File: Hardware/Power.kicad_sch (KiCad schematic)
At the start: 43 parts, among them J2 S2B-PH-SM4-TB, Q1 DMP3099L, Q2 2N7002, Q3 2N7002, SW4 KMR231NG, SW5 KSS3xxGx, U2 AP2112K-3.3, U3 BQ21040DBV

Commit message: sch: flip battery connector. The connector did not align with the pinout of the battery, requiring us to flip the connector. CAUTION: If upgrading from Terra X01 to X02, flip back the connector leads on your battery!
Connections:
- net GND: now also J2.2 (Pin_2); no longer J2.1 (Pin_1)
- net VBAT: now also J2.1 (Pin_1); no longer J2.2 (Pin_2)
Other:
- moved on the sheet: J2
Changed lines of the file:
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@@
 	(wire
 		(pts
-			(xy 44.45 101.6) (xy 44.45 102.87)
-		)
-		(stroke
-			(width 0)
-			(type default)
-		)
-	)
-	(wire
-		(pts
 			(xy 147.32 110.49) (xy 147.32 114.3)
 		)
@@
 	(wire
 		(pts
-			(xy 49.53 101.6) (xy 44.45 101.6)
-		)
-		(stroke
-			(width 0)
-			(type default)
-		)
-	)
-	(wire
-		(pts
 			(xy 68.58 132.08) (xy 68.58 133.35)
 		)
@@
 	(wire
 		(pts
-			(xy 49.53 102.87) (xy 49.53 101.6)
-		)
-		(stroke
-			(width 0)
-			(type default)
-		)
-	)
-	(wire
-		(pts
 			(xy 182.88 52.07) (xy 185.42 52.07)
 		)
@@
 	(symbol
 		(lib_id "Connector_Generic_MountingPin:Conn_01x02_MountingPin")
-		(at 49.53 110.49 180)
+		(at 49.53 107.95 0)
+		(mirror y)
 		(unit 1)
 		(exclude_from_sim no)
@@
 		(dnp no)
 		(property "Reference" "J2"
-			(at 46.99 110.1345 0)
+			(at 46.99 108.3055 0)
 			(effects
 				(font
@@
 		)
 		(property "Value" "S2B-PH-SM4-TB"
-			(at 46.99 107.5945 0)
+			(at 46.99 110.8455 0)
 			(effects
 				(font
@@
 		)
 		(property "Footprint" "Connector_JST:JST_PH_S2B-PH-SM4-TB_1x02-1MP_P2.00mm_Horizontal"
-			(at 49.53 110.49 0)
+			(at 49.53 107.95 0)
 			(effects
 				(font
@@
 		)
 		(property "Datasheet" "~"
-			(at 49.53 110.49 0)
+			(at 49.53 107.95 0)
 			(effects
 				(font
@@
 		)
 		(property "Description" "Generic connectable mounting pin connector, single row, 01x02, script generated (kicad-library-utils/schlib/autogen/connector/)"
-			(at 49.53 110.49 0)
+			(at 49.53 107.95 0)
 			(effects
 				(font
@@
 		)
 		(property "MPN" "S2B-PH-SM4-TB"
-			(at 49.53 110.49 0)
+			(at 49.53 107.95 0)
 			(effects
 				(font
@@
 		)
 		(instances
-			(project ""
+			(project "Terra-HW"
 				(path "/acca4a2f-1cc7-44b0-a26a-921257f6c268/5f0d062d-9fa8-4c48-be05-0b92e4e6324b"
 					(reference "J2")
@@
 	(symbol
 		(lib_id "power:GND")
-		(at 44.45 102.87 0)
+		(at 49.53 115.57 0)
 		(unit 1)
 		(exclude_from_sim no)
@@
 		(fields_autoplaced yes)
 		(property "Reference" "#PWR023"
-			(at 44.45 109.22 0)
+			(at 49.53 121.92 0)
 			(effects
 				(font
@@
 		)
 		(property "Value" "GND"
-			(at 44.45 107.95 0)
+			(at 49.53 120.65 0)
 			(effects
 				(font
@@
 		)
 		(property "Footprint" ""
-			(at 44.45 102.87 0)
+			(at 49.53 115.57 0)
 			(effects
 				(font
@@
 		)
 		(property "Datasheet" ""
-			(at 44.45 102.87 0)
+			(at 49.53 115.57 0)
 			(effects
 				(font
@@
 		)
 		(property "Description" "Power symbol creates a global label with name \"GND\" , ground"
-			(at 44.45 102.87 0)
+			(at 49.53 115.57 0)
 			(effects
 				(font

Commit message: sch: replace gps for TESSO-LIV3R
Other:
- note added: "TODO: Fix shutdown issue from stray voltage at this node."
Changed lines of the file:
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@@
+		)
+	)
+	(text "TODO: Fix shutdown issue from stray voltage at this node."
+		(exclude_from_sim no)
+		(at 116.332 38.862 0)
+		(effects
+			(font
+				(size 1.27 1.27)
+				(thickness 0.254)
+				(bold yes)
+				(color 255 153 0 1)
+			)
 		)
 	)

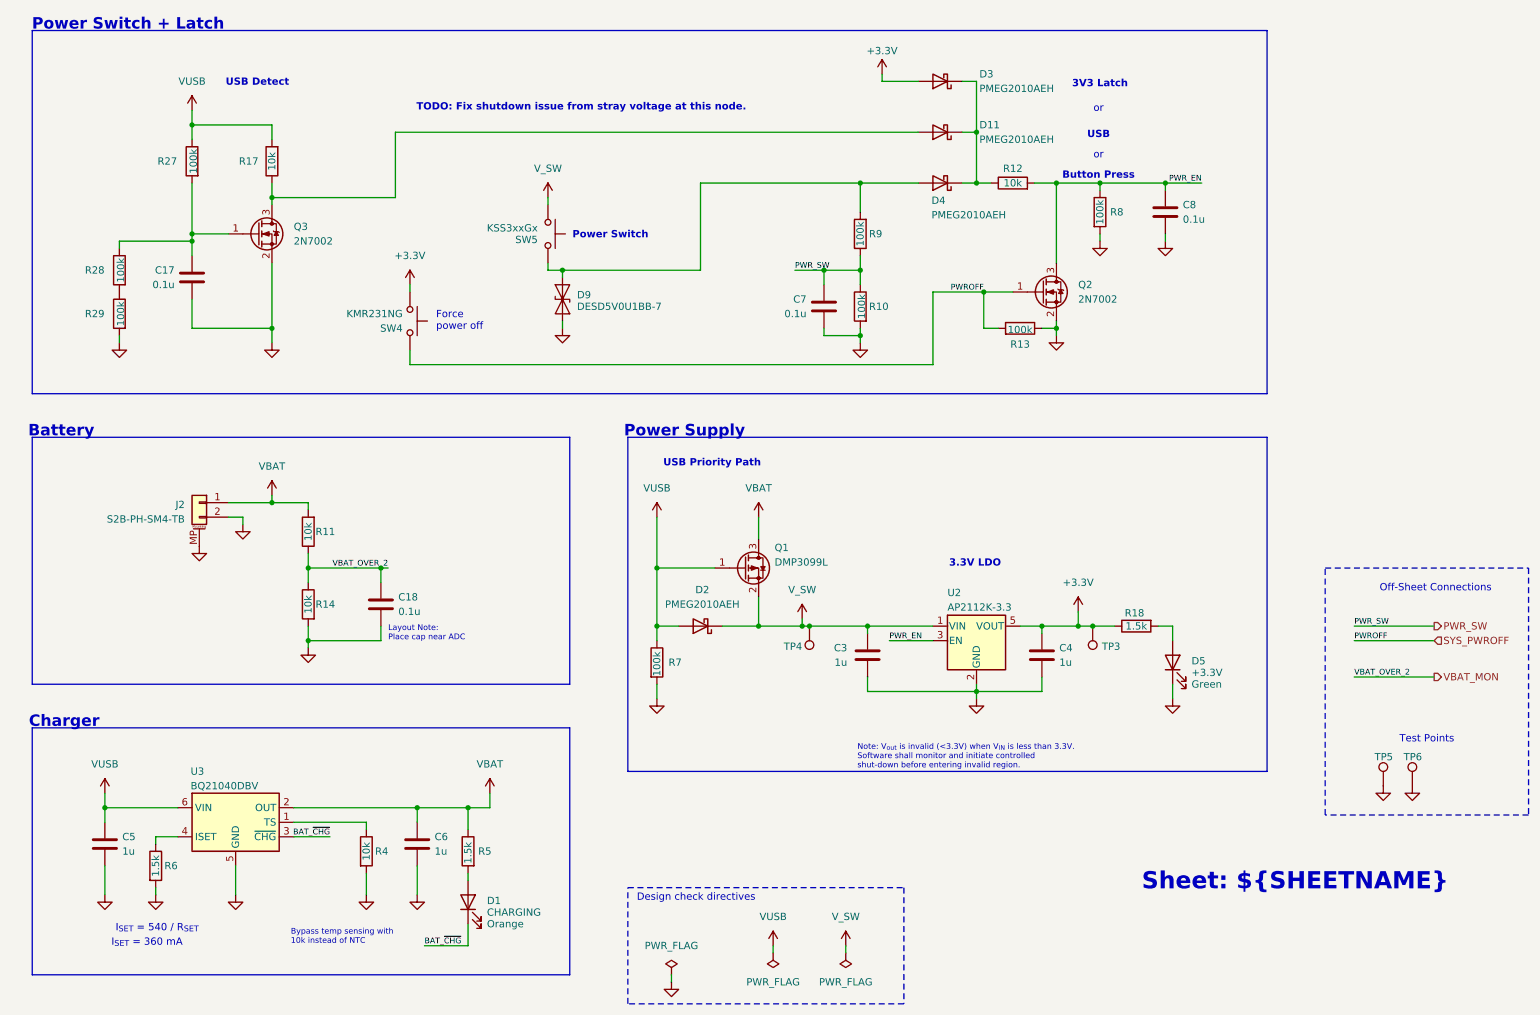
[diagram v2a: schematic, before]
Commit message: sch: change USB Detect to SN74LVC1G14
Removed N-FET used, which had a problem of restarting the device
after powerdown when only powered by battery (no USB)
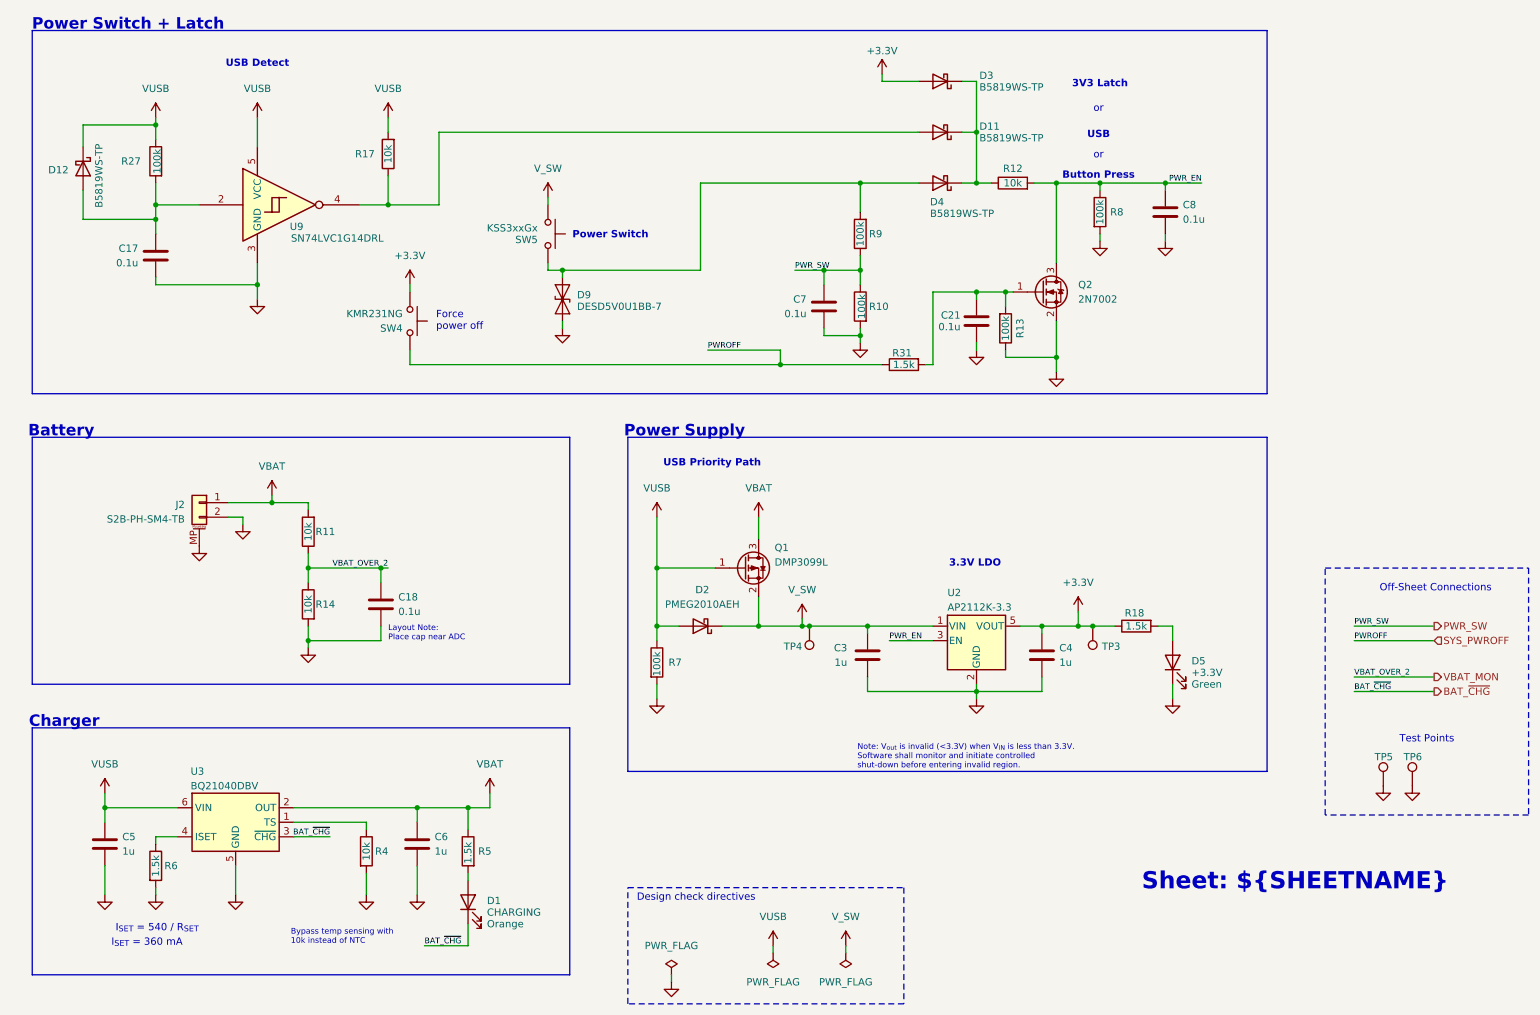
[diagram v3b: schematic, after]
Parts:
- removed Q3: 2N7002, Package_TO_SOT_SMD:SOT-23, symbol Transistor_FET:2N7002
- removed R28, R29: 100k, Resistor_SMD:R_0603_1608Metric, symbol Device:R
- added C21: 0.1u, Capacitor_SMD:C_0603_1608Metric, symbol Device:C
- added D12: B5819WS-TP, Diode_SMD:D_SOD-323, symbol Diode:MBR0520
- added R31: 1.5k, Resistor_SMD:R_0603_1608Metric, symbol Device:R
- added U9: SN74LVC1G14DRL, Package_TO_SOT_SMD:SOT-553, symbol 74xGxx:SN74LVC1G14DRL
- D11, D3, D4: value PMEG2010AEH -> B5819WS-TP; footprint Diode_SMD:D_SOD-123 -> Diode_SMD:D_SOD-323; MPN PMEG2010AEH -> B5819WS-TP
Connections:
- net GND: now also C21.2, U9.3 (GND)
- net SYS_PWROFF: now also R31.1; no longer Q2.1 (G), R13.2
- net VUSB: now also D12.1 (K), U9.5 (VCC)
- net at C17.1, R27.2: now also D12.2 (A), U9.2
- net at D11.2 (A), R17.1: now also U9.4
- new net: C21.1, Q2.1 (G), R13.2, R31.2
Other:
- note removed: "TODO: Fix shutdown issue from stray voltage at this node."
- moved on the sheet: R13

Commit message: sch: updates
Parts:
- R11, R14: value 10k -> 100k; MPN RC0603FR-0710KL -> RC0603FR-07100KL
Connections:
- net GND: now also R14.1; no longer R14.2
- net VBAT_MON: now also R14.2; no longer R14.1
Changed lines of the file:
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@@
 	(title_block
 		(title "${TITLE}")
-		(date "2025-04-06")
+		(date "2025-08-29")
 		(rev "${REVISION}")
 		(company "${COMPANY}")
@@
 	)
 	(symbol
-		(lib_id "Device:R")
-		(at 68.58 125.73 0)
-		(mirror y)
-		(unit 1)
-		(exclude_from_sim no)
-		(in_bom yes)
-		(on_board yes)
-		(dnp no)
-		(property "Reference" "R14"
-			(at 69.85 125.73 0)
-			(effects
-				(font
-					(size 1.27 1.27)
-				)
-				(justify right)
-			)
-		)
-		(property "Value" "10k"
-			(at 68.58 125.73 90)
-			(effects
-				(font
-					(size 1.27 1.27)
-				)
-			)
-		)
-		(property "Footprint" "Resistor_SMD:R_0603_1608Metric"
-			(at 70.358 125.73 90)
-			(effects
-				(font
-					(size 1.27 1.27)
-				)
-				(hide yes)
-			)
-		)
-		(property "Datasheet" "https://www.lcsc.com/datasheet/lcsc_datasheet_2304140030_YAGEO-RC0603FR-071KL_C22548.pdf"
-			(at 68.58 125.73 0)
-			(effects
-				(font
-					(size 1.27 1.27)
-				)
-				(hide yes)
-			)
-		)
-		(property "Description" "Resistor"
-			(at 68.58 125.73 0)
-			(effects
-				(font
-					(size 1.27 1.27)
-				)
-				(hide yes)
-			)
-		)
-		(property "MPN" "RC0603FR-0710KL"
-			(at 68.58 125.73 0)
-			(effects
-				(font
-					(size 1.27 1.27)
-				)
-				(hide yes)
-			)
-		)
-		(pin "1"
-		)
-		(pin "2"
-		)
-		(instances
-			(project "Terra-HW"
-				(path "/acca4a2f-1cc7-44b0-a26a-921257f6c268/5f0d062d-9fa8-4c48-be05-0b92e4e6324b"
-					(reference "R14")
-					(unit 1)
-				)
-			)
-		)
-	)
-	(symbol
 		(lib_id "power:VBUS")
 		(at 129.54 110.49 0)
@@
 	)
 	(symbol
+		(lib_id "Device:R")
+		(at 68.58 125.73 180)
+		(unit 1)
+		(exclude_from_sim no)
+		(in_bom yes)
+		(on_board yes)
+		(dnp no)
+		(property "Reference" "R14"
+			(at 70.104 125.73 0)
+			(effects
+				(font
+					(size 1.27 1.27)
+				)
+				(justify right)
+			)
+		)
+		(property "Value" "100k"
+			(at 68.58 125.73 90)
+			(effects
+				(font
+					(size 1.27 1.27)
+				)
+			)
+		)
+		(property "Footprint" "Resistor_SMD:R_0603_1608Metric"
+			(at 70.358 125.73 90)
+			(effects
+				(font
+					(size 1.27 1.27)
+				)
+				(hide yes)
+			)
+		)
+		(property "Datasheet" "https://www.lcsc.com/datasheet/lcsc_datasheet_2304140030_YAGEO-RC0603FR-071KL_C22548.pdf"
+			(at 68.58 125.73 0)
+			(effects
+				(font
+					(size 1.27 1.27)
+				)
+				(hide yes)
+			)
+		)
+		(property "Description" "Resistor"
+			(at 68.58 125.73 0)
+			(effects
+				(font
+					(size 1.27 1.27)
+				)
+				(hide yes)
+			)
+		)
+		(property "MPN" "RC0603FR-07100KL"
+			(at 68.58 125.73 0)
+			(effects
+				(font
+					(size 1.27 1.27)
+				)
+				(hide yes)
+			)
+		)
+		(pin "1"
+		)
+		(pin "2"
+		)
+		(instances
+			(project "Terra-HW"
+				(path "/acca4a2f-1cc7-44b0-a26a-921257f6c268/5f0d062d-9fa8-4c48-be05-0b92e4e6324b"
+					(reference "R14")
+					(unit 1)
+				)
+			)
+		)
+	)
+	(symbol
 		(lib_id "Diode:MBR0520")
 		(at 179.07 43.18 180)
@@
 	)
 	(symbol
+		(lib_id "Device:R")
+		(at 68.58 113.03 180)
+		(unit 1)
+		(exclude_from_sim no)
+		(in_bom yes)
+		(on_board yes)
+		(dnp no)
+		(property "Reference" "R11"
+			(at 70.104 113.03 0)
+			(effects
+				(font
+					(size 1.27 1.27)
+				)
+				(justify right)
+			)
+		)
+		(property "Value" "100k"
+			(at 68.58 113.03 90)
+			(effects
+				(font
+					(size 1.27 1.27)
+				)
+			)
+		)
+		(property "Footprint" "Resistor_SMD:R_0603_1608Metric"
+			(at 70.358 113.03 90)
+			(effects
+				(font
+					(size 1.27 1.27)
+				)
+				(hide yes)
+			)
+		)
+		(property "Datasheet" "https://www.lcsc.com/datasheet/lcsc_datasheet_2304140030_YAGEO-RC0603FR-071KL_C22548.pdf"
+			(at 68.58 113.03 0)
+			(effects
+				(font
+					(size 1.27 1.27)
+				)
+				(hide yes)
+			)
+		)
+		(property "Description" "Resistor"
+			(at 68.58 113.03 0)
+			(effects
+				(font
+					(size 1.27 1.27)
+				)
+				(hide yes)
+			)
+		)
+		(property "MPN" "RC0603FR-07100KL"
+			(at 68.58 113.03 0)
+			(effects
+				(font
+					(size 1.27 1.27)
+				)
+				(hide yes)
+			)
+		)
+		(pin "1"
+		)
+		(pin "2"
+		)
+		(instances
+			(project "Terra-HW"
+				(path "/acca4a2f-1cc7-44b0-a26a-921257f6c268/5f0d062d-9fa8-4c48-be05-0b92e4e6324b"
+					(reference "R11")
+					(unit 1)
+				)
+			)
+		)
+	)
+	(symbol
 		(lib_id "power:GND")
 		(at 49.53 115.57 0)
@@
 					(unit 1)
 				)
-			)
-		)
-	)
-	(symbol
-		(lib_id "Device:R")
-		(at 68.58 113.03 180)
-		(unit 1)
-		(exclude_from_sim no)
-		(in_bom yes)
-		(on_board yes)
-		(dnp no)
-		(property "Reference" "R11"
-			(at 69.85 113.03 0)
-			(effects
-				(font
-					(size 1.27 1.27)
-				)
-				(justify right)
-			)
-		)
-		(property "Value" "10k"
-			(at 68.58 113.03 90)
-			(effects
-				(font
-					(size 1.27 1.27)
-				)
-			)
-		)
-		(property "Footprint" "Resistor_SMD:R_0603_1608Metric"
-			(at 70.358 113.03 90)
-			(effects
-				(font
-					(size 1.27 1.27)
-				)
-				(hide yes)
-			)
-		)
-		(property "Datasheet" "https://www.lcsc.com/datasheet/lcsc_datasheet_2304140030_YAGEO-RC0603FR-071KL_C22548.pdf"
-			(at 68.58 113.03 0)
-			(effects
-				(font
-					(size 1.27 1.27)
-				)
-				(hide yes)
-			)
-		)
-		(property "Description" "Resistor"
-			(at 68.58 113.03 0)
-			(effects
-				(font
-					(size 1.27 1.27)
-				)
-				(hide yes)
-			)
-		)
-		(property "MPN" "RC0603FR-0710KL"
-			(at 68.58 113.03 0)
-			(effects
-				(font
-					(size 1.27 1.27)
-				)
-				(hide yes)
-			)
-		)
-		(pin "1"
-		)
-		(pin "2"
-		)
-		(instances
-			(project "Terra-HW"
-				(path "/acca4a2f-1cc7-44b0-a26a-921257f6c268/5f0d062d-9fa8-4c48-be05-0b92e4e6324b"
-					(reference "R11")
-					(unit 1)
-				)

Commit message: sch/pb: tweaks for X02-001 release, submit to vendor
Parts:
- U9: Alt1 (none) -> 74LVC1G14Z-7; MPN (none) -> SN74LVC1G14DRL
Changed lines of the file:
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@@
+			)
+		)
+		(property "MPN" "SN74LVC1G14DRL"
+			(at 64.77 55.88 0)
+			(effects
+				(font
+					(size 1.27 1.27)
+				)
+				(hide yes)
+			)
+		)
+		(property "Alt1" "74LVC1G14Z-7"
+			(at 64.77 55.88 0)
+			(effects
+				(font
+					(size 1.27 1.27)
+				)
+				(hide yes)
 			)
 		)

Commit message: prepare export for Rev A
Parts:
- D5: MPN LTST-C190GKT -> IN-S63AT5UW; now not fitted
- R18: now not fitted
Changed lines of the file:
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@@
 	(title_block
 		(title "${TITLE}")
-		(date "2025-08-29")
+		(date "2025-11-18")
 		(rev "${REVISION}")
 		(company "${COMPANY}")
@@
 		(in_bom yes)
 		(on_board yes)
-		(dnp no)
+		(dnp yes)
 		(property "Reference" "R18"
 			(at 211.328 127.254 90)
@@
 	)
 	(symbol
+		(lib_id "Device:LED")
+		(at 219.71 135.89 90)
+		(unit 1)
+		(exclude_from_sim no)
+		(in_bom yes)
+		(on_board yes)
+		(dnp yes)
+		(property "Reference" "D5"
+			(at 223.012 135.636 90)
+			(effects
+				(font
+					(size 1.27 1.27)
+				)
+				(justify right)
+			)
+		)
+		(property "Value" "+3.3V"
+			(at 223.012 137.668 90)
+			(effects
+				(font
+					(size 1.27 1.27)
+				)
+				(justify right)
+			)
+		)
+		(property "Footprint" "Diode_SMD:D_0603_1608Metric"
+			(at 219.71 135.89 0)
+			(effects
+				(font
+					(size 1.27 1.27)
+				)
+				(hide yes)
+			)
+		)
+		(property "Datasheet" "https://www.inolux-corp.com/datasheet/SMDLED/Mono%20Color%20Top%20View/IN-S63AT%20Series_V1.4.pdf"
+			(at 219.71 135.89 0)
+			(effects
+				(font
+					(size 1.27 1.27)
+				)
+				(hide yes)
+			)
+		)
+		(property "Description" "White"
+			(at 223.012 139.7 90)
+			(effects
+				(font
+					(size 1.27 1.27)
+				)
+				(justify right)
+			)
+		)
+		(property "Sim.Pins" "1=K 2=A"
+			(at 219.71 135.89 0)
+			(effects
+				(font
+					(size 1.27 1.27)
+				)
+				(hide yes)
+			)
+		)
+		(property "MPN" "IN-S63AT5UW"
+			(at 219.71 135.89 90)
+			(effects
+				(font
+					(size 1.27 1.27)
+				)
+				(hide yes)
+			)
+		)
+		(pin "2"
+		)
+		(pin "1"
+		)
+		(instances
+			(project "Terra-HW"
+				(path "/acca4a2f-1cc7-44b0-a26a-921257f6c268/5f0d062d-9fa8-4c48-be05-0b92e4e6324b"
+					(reference "D5")
+					(unit 1)
+				)
+			)
+		)
+	)
+	(symbol
 		(lib_id "Regulator_Linear:AP2112K-3.3")
 		(at 185.42 132.08 0)
@@
 					(unit 1)
 				)
-			)
-		)
-	)
-	(symbol
-		(lib_id "Device:LED")
-		(at 219.71 135.89 90)
-		(unit 1)
-		(exclude_from_sim no)
-		(in_bom yes)
-		(on_board yes)
-		(dnp no)
-		(property "Reference" "D5"
-			(at 223.012 135.636 90)
-			(effects
-				(font
-					(size 1.27 1.27)
-				)
-				(justify right)
-			)
-		)
-		(property "Value" "+3.3V"
-			(at 223.012 137.668 90)
-			(effects
-				(font
-					(size 1.27 1.27)
-				)
-				(justify right)
-			)
-		)
-		(property "Footprint" "Diode_SMD:D_0603_1608Metric"
-			(at 219.71 135.89 0)
-			(effects
-				(font
-					(size 1.27 1.27)
-				)
-				(hide yes)
-			)
-		)
-		(property "Datasheet" "https://mm.digikey.com/Volume0/opasdata/d220001/medias/docus/858/LTST-C190GKT.pdf"
-			(at 219.71 135.89 0)
-			(effects
-				(font
-					(size 1.27 1.27)
-				)
-				(hide yes)
-			)
-		)
-		(property "Description" "Green"
-			(at 223.012 139.7 90)
-			(effects
-				(font
-					(size 1.27 1.27)
-				)
-				(justify right)
-			)
-		)
-		(property "Sim.Pins" "1=K 2=A"
-			(at 219.71 135.89 0)
-			(effects
-				(font
-					(size 1.27 1.27)
-				)
-				(hide yes)
-			)
-		)
-		(property "MPN" "LTST-C190GKT"
-			(at 219.71 135.89 90)
-			(effects
-				(font
-					(size 1.27 1.27)
-				)
-				(hide yes)
-			)
-		)
-		(pin "2"
-		)
-		(pin "1"
-		)
-		(instances
-			(project "Terra-HW"
-				(path "/acca4a2f-1cc7-44b0-a26a-921257f6c268/5f0d062d-9fa8-4c48-be05-0b92e4e6324b"
-					(reference "D5")
-					(unit 1)
-				)

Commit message: update BOM items to full P/N from previous PCB order feedback
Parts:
- D2: MPN PMEG2010AEH -> PMEG2010AEH,115
- U3: MPN BQ21040DBV -> BQ21040DBVR
- U9: MPN SN74LVC1G14DRL -> SN74LVC1G14DRLR
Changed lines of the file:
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@@
 			)
 		)
-		(property "MPN" "BQ21040DBV"
+		(property "MPN" "BQ21040DBVR"
 			(at 55.88 163.83 0)
 			(effects
@@
 			)
 		)
-		(property "MPN" "SN74LVC1G14DRL"
+		(property "MPN" "SN74LVC1G14DRLR"
 			(at 64.77 55.88 0)
 			(effects
@@
 			)
 		)
-		(property "MPN" "PMEG2010AEH"
+		(property "MPN" "PMEG2010AEH,115"
 			(at 137.16 129.54 0)
 			(effects
